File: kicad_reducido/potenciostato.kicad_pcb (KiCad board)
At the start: 2 copper layers, 100 x 100 mm, 36 parts, among them J1 Conn_01x03_Female, J2 USB_B_Micro, J3 Conn_01x03_Male, U1 OP77, U2 TL082, U3 OP77, U4 OP77, U7 TL064

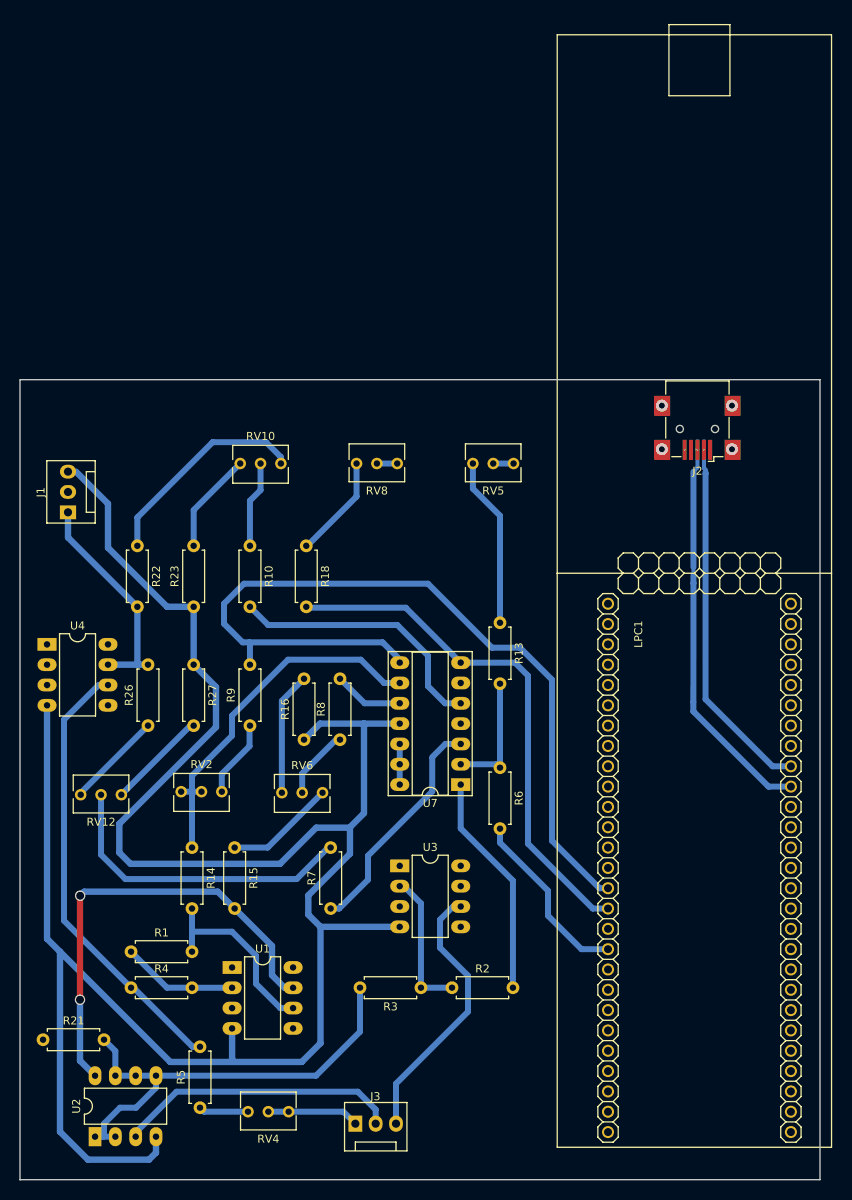
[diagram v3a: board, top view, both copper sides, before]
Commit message: pcb reducido listo falta revisar
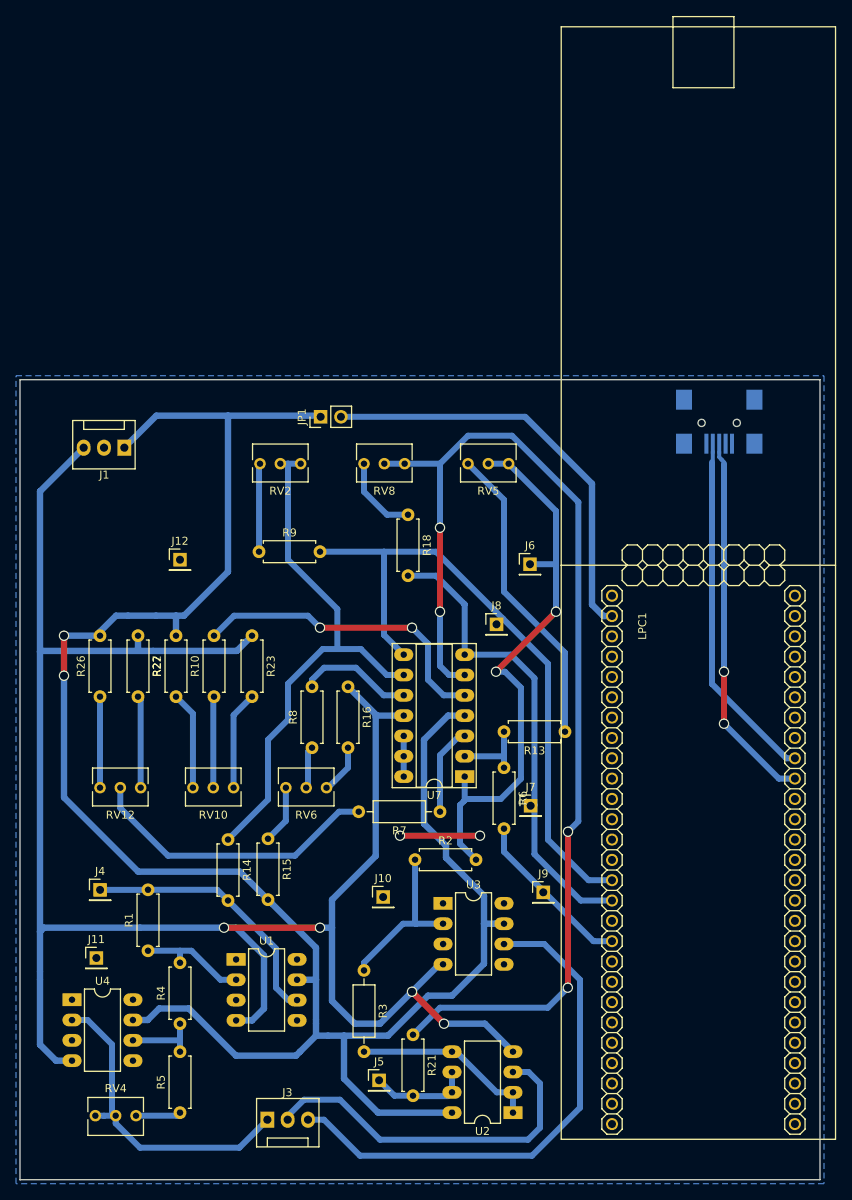
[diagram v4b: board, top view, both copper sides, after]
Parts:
- added J10: Conn_01x01_Female, Connector_PinHeader_2.54mm:PinHeader_1x01_P2.54mm_Vertical, F.Cu at (745.4, 67.2)
- added J11: Conn_01x01_Female, Connector_PinHeader_2.54mm:PinHeader_1x01_P2.54mm_Vertical, F.Cu at (709.5, 74.8)
- added J12: Conn_01x01_Female, Connector_PinHeader_2.54mm:PinHeader_1x01_P2.54mm_Vertical, F.Cu at (720.0, 25.0)
- added J4: Conn_01x01_Female, Connector_PinHeader_2.54mm:PinHeader_1x01_P2.54mm_Vertical, F.Cu at (710.0, 66.3)
- added J5: Conn_01x01_Female, Connector_PinHeader_2.54mm:PinHeader_1x01_P2.54mm_Vertical, F.Cu at (744.9, 90.1)
- added J6: Conn_01x01_Female, Connector_PinHeader_2.54mm:PinHeader_1x01_P2.54mm_Vertical, F.Cu at (763.8, 25.6)
- added J7: Conn_01x01_Female, Connector_PinHeader_2.54mm:PinHeader_1x01_P2.54mm_Vertical, F.Cu at (763.8, 55.8)
- added J8: Conn_01x01_Female, Connector_PinHeader_2.54mm:PinHeader_1x01_P2.54mm_Vertical, F.Cu at (759.6, 33.1)
- added J9: Conn_01x01_Female, Connector_PinHeader_2.54mm:PinHeader_1x01_P2.54mm_Vertical, F.Cu at (765.4, 66.6)
- added JP1: Jumper, Connector_PinHeader_2.54mm:PinHeader_1x02_P2.54mm_Vertical, F.Cu at (737.6, 7.14)
- J2: moved to B.Cu
- R3, R7: footprint Resistor_THT:R_Axial_DIN0207_L6.3mm_D2.5mm_P7.62mm_Horizontal -> Resistor_THT:R_Axial_DIN0207_L6.3mm_D2.5mm_P10.16mm_Horizontal
- moved U2 52.3 mm to (761.6, 94.1), turned to 180 degrees
- moved R21 46.2 mm to (749.1, 84.4), turned to 270 degrees
- moved U4 44.5 mm to (706.5, 80.0)
- moved RV10 42.0 mm to (721.6, 53.5), turned to 180 degrees
- moved RV2 41.3 mm to (730.0, 13.0), turned to 180 degrees
- moved R9 21.8 mm to (729.9, 24.0), turned to 0 degrees
- moved R22 19.5 mm to (719.5, 42.1), turned to 90 degrees
- moved R10 19.4 mm to (724.2, 42.1), turned to 90 degrees
- moved R7 18.3 mm to (752.5, 56.5), turned to 180 degrees
- moved R2 16.7 mm to (749.4, 62.5)
- moved R13 15.9 mm to (768.1, 46.5), turned to 180 degrees
- moved RV4 14.0 mm to (714.5, 94.5), turned to 0 degrees
- moved R18 13.3 mm to (748.5, 19.4)
- moved J3 11.0 mm to (730.9, 95.0)
- moved J1 10.7 mm to (713.0, 11.0), turned to 180 degrees
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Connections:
- J2 pad 1: (no net) -> Net-(J2-Pad1)
- J2 pad 4: (no net) -> Net-(J2-Pad4)
- LPC1 pad 1: (no net) -> GND
- LPC1 pad 10: (no net) -> Net-(LPC1-Pad10)
- LPC1 pad 11: (no net) -> Net-(LPC1-Pad11)
- LPC1 pad 12: (no net) -> Net-(LPC1-Pad12)
- LPC1 pad 13: (no net) -> Net-(LPC1-Pad13)
- LPC1 pad 14: (no net) -> Net-(LPC1-Pad14)
- LPC1 pad 17: (no net) -> Net-(LPC1-Pad17)
- LPC1 pad 19: (no net) -> Net-(LPC1-Pad19)
- LPC1 pad 2: +5V -> Net-(JP1-Pad2)
- LPC1 pad 20: (no net) -> Net-(LPC1-Pad20)
- LPC1 pad 21: (no net) -> Net-(LPC1-Pad21)
- LPC1 pad 22: (no net) -> Net-(LPC1-Pad22)
- LPC1 pad 23: (no net) -> Net-(LPC1-Pad23)
- LPC1 pad 24: (no net) -> Net-(LPC1-Pad24)
- LPC1 pad 25: (no net) -> Net-(LPC1-Pad25)
- LPC1 pad 26: (no net) -> Net-(LPC1-Pad26)
- LPC1 pad 27: (no net) -> Net-(LPC1-Pad27)
- LPC1 pad 28: (no net) -> Net-(LPC1-Pad28)
- LPC1 pad 29: (no net) -> Net-(LPC1-Pad29)
- LPC1 pad 3: (no net) -> Net-(LPC1-Pad3)
- LPC1 pad 30: (no net) -> Net-(LPC1-Pad30)
- LPC1 pad 31: (no net) -> Net-(LPC1-Pad31)
- LPC1 pad 32: (no net) -> Net-(LPC1-Pad32)
- LPC1 pad 33: (no net) -> Net-(LPC1-Pad33)
- LPC1 pad 34: (no net) -> Net-(LPC1-Pad34)
- LPC1 pad 35: (no net) -> Net-(LPC1-Pad35)
- LPC1 pad 38: (no net) -> Net-(LPC1-Pad38)
- LPC1 pad 39: (no net) -> Net-(LPC1-Pad39)
- LPC1 pad 4: (no net) -> Net-(LPC1-Pad4)
- LPC1 pad 40: (no net) -> Net-(LPC1-Pad40)
- LPC1 pad 41: (no net) -> Net-(LPC1-Pad41)
- LPC1 pad 42: (no net) -> Net-(LPC1-Pad42)
- LPC1 pad 43: (no net) -> Net-(LPC1-Pad43)
- LPC1 pad 44: (no net) -> Net-(LPC1-Pad44)
- LPC1 pad 45: (no net) -> Net-(LPC1-Pad45)
- LPC1 pad 46: (no net) -> Net-(LPC1-Pad46)
- LPC1 pad 47: (no net) -> Net-(LPC1-Pad47)
- LPC1 pad 48: (no net) -> Net-(LPC1-Pad48)
- LPC1 pad 49: (no net) -> Net-(LPC1-Pad49)
- LPC1 pad 5: (no net) -> Net-(LPC1-Pad5)
- LPC1 pad 50: (no net) -> Net-(LPC1-Pad50)
- LPC1 pad 51: (no net) -> Net-(LPC1-Pad51)
- LPC1 pad 52: (no net) -> Net-(LPC1-Pad52)
- LPC1 pad 53: (no net) -> Net-(LPC1-Pad53)
- LPC1 pad 6: (no net) -> Net-(LPC1-Pad6)
- LPC1 pad 7: (no net) -> Net-(LPC1-Pad7)
- LPC1 pad 8: (no net) -> Net-(LPC1-Pad8)
- LPC1 pad 9: (no net) -> Net-(LPC1-Pad9)
- U1 pad 1: (no net) -> Net-(U1-Pad1)
- U1 pad 5: (no net) -> Net-(U1-Pad5)
- U1 pad 8: (no net) -> Net-(U1-Pad8)
- U3 pad 1: (no net) -> Net-(U3-Pad1)
- U3 pad 5: (no net) -> Net-(U3-Pad5)
- U3 pad 8: (no net) -> Net-(U3-Pad8)
- U4 pad 1: (no net) -> Net-(U4-Pad1)
- U4 pad 5: (no net) -> Net-(U4-Pad5)
- U4 pad 8: (no net) -> Net-(U4-Pad8)
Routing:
- net +5V: track 84.9 -> 260.2 mm
- net Net-(R21-Pad1): track 2.54 -> 141.6 mm, vias 0 -> 4
- net Net-(JP1-Pad2): track 0.00 -> 53.1 mm
- net Net-(R4-Pad1): track 56.5 -> 9.41 mm
- net /salida_dac/VIN: track 30.6 -> 72.3 mm, vias 0 -> 2
- net Net-(J3-Pad3): track 33.9 -> 65.7 mm
- net Net-(J3-Pad1): track 11.5 -> 40.5 mm
- net -5V: track 272.6 -> 245.9 mm, vias 0 -> 4
- net Net-(R3-Pad2): track 49.8 -> 23.3 mm
- net /LPC/ADC0: track 106.1 -> 81.8 mm
- net Net-(R14-Pad1): track 46.2 -> 68.5 mm
- net Net-(R7-Pad1): track 28.9 -> 11.1 mm
- net Net-(R13-Pad1): track 21.3 -> 38.5 mm
- net Net-(R22-Pad1): track 27.2 -> 12.3 mm
- net GND: track 5.08 -> 15.1 mm, vias 5 -> 2
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- added copper zone on B.Cu, net GND
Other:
- net class USB: trace_width 0.75 -> 0.5; via_dia 1.3 -> 0.7; via_drill 1 -> 0.5

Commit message: cambio huella usb
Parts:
- J2: footprint Connector_USB:USB_Mini-B_Wuerth_65100516121_Horizontal -> Connector_USB:USB_Mini-B_Tensility_54-00023_Vertical; moved to F.Cu
- moved J12 629.3 mm to (92.9, 77.5)
- moved J4 629.3 mm to (82.9, 118.8)
- moved J5 629.3 mm to (117.8, 142.6)
- moved J6 629.3 mm to (136.6, 78.1)
- moved J7 629.3 mm to (136.7, 108.2)
- moved J9 629.3 mm to (138.3, 119.1)
- moved JP1 629.3 mm to (110.5, 59.6)
- moved LPC1 629.3 mm to (152.6, 48.3)
- moved R1 629.3 mm to (88.9, 126.4)
- moved R10 629.3 mm to (97.1, 94.6)
- moved R13 629.3 mm to (141.0, 99.0)
- moved R14 629.3 mm to (98.9, 112.5)
- moved R15 629.3 mm to (103.9, 112.4)
- moved R16 629.3 mm to (113.9, 93.4)
- moved R18 629.3 mm to (121.4, 71.9)
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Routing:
- net Net-(J2-Pad3): track 45.9 -> 48.9 mm, vias 2 -> 0
- net Net-(J2-Pad2): track 43.4 -> 44.8 mm

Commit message: delay por timer en adc
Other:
- net class Alimentación removed
- net class Default removed
- net class Señal removed
- net class USB removed

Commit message: agregado lo de Hernan y fixeado el kicad pcb
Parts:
- J2: footprint Connector_USB:USB_Mini-B_Tensility_54-00023_Vertical -> Connector_USB:USB_Mini-B_Wuerth_65100516121_Horizontal; moved to B.Cu
- R15, R22: value 10K -> 0
- R16, RV10, RV6: value 1K -> 10K
- R23: value 15K -> 10K
- moved J12 629.3 mm to (720.0, 25.0)
- moved J4 629.3 mm to (710.0, 66.3)
- moved J5 629.3 mm to (744.9, 90.1)
- moved J6 629.3 mm to (763.8, 25.6)
- moved J7 629.3 mm to (763.8, 55.8)
- moved J9 629.3 mm to (765.4, 66.6)
- moved JP1 629.3 mm to (737.6, 7.14)
- moved LPC1 629.3 mm to (779.7, -4.15)
- moved R1 629.3 mm to (716.0, 73.9)
- moved R10 629.3 mm to (724.2, 42.1)
- moved R13 629.3 mm to (768.1, 46.5)
- moved R14 629.3 mm to (726.0, 60.0)
- moved R15 629.3 mm to (731.0, 59.9)
- moved R16 629.3 mm to (741.0, 40.9)
- moved R18 629.3 mm to (748.5, 19.4)
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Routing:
- net Net-(J2-Pad3): track 48.9 -> 45.9 mm, vias 0 -> 2
- net Net-(J2-Pad2): track 44.8 -> 43.4 mm
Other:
- net class Alimentación added: clearance 0.7, trace_width 0.8, via_dia 1.3, via_drill 1
- net class Default added: clearance 0.7, trace_width 0.75, via_dia 1.3, via_drill 1
- net class Señal added: clearance 0.5, trace_width 0.75, via_dia 1.3, via_drill 1
- net class USB added: clearance 0.2, trace_width 0.5, via_dia 0.7, via_drill 0.5

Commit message: actualizado pcb desde esquematico al poner Rs de 10k y actualizar sus valores en funcion a la placa ya hecha
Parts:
- R1: value 15K -> 33K
- R10: renamed from R27; value 1K -> 10K
- R11: renamed from R14; value 1K -> 10K
- R12: renamed from R8; value 1K -> 10K
- R13: value 4K7 -> 6K8
- R14: renamed from R15; value 0 -> 10K
- R15: renamed from R16; value 10K -> 1K
- R17: renamed from R21; value 1K -> 10K
- R18: renamed from R10; value 1K -> 10K
- R19: renamed from R22; value 0 -> 10K
- R20: renamed from R23; value 10K -> 15K
- R4: value 1K -> 10K
- R5: value 1M -> 0K
- R6: renamed from R26; value 10K -> 8.2K
- R7: renamed from R6; value 1K -> 10K
- R8: renamed from R7; value 1K -> 10K
- RV4: renamed from RV5; value R_POT -> 1K
- RV5: renamed from RV6; value 10K -> 1K
- RV7: renamed from RV10; value 10K -> 1K
- renumbered J10 to J1, J8 to J10, J9 to J11, J2 to J12, J11 to J2, J1 to J3, J12 to J4, J4 to J5, J5 to J6, J6 to J7, J3 to J8, J7 to J9, R18 to R16, RV4 to RV1, RV12 to RV2, RV2 to RV3, RV8 to RV6, U7 to U5
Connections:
- J8 pad 2: Net-(J3-Pad2) -> Net-(J8-Pad2)
